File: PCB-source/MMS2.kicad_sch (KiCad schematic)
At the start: 4 parts

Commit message: ch32
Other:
- added sheet CH32V003 (CH32V003.kicad_sch)
- sheet MCU ports: added none; removed CAN_AUTOTERM{1,2}
- sheet STlink-BMprobe ports: added STLINK{UART}; removed none

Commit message: Component placement done
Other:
- sheet Interboard_connector ports: added Altmode[1..16], Chainbus_I2C_addr[0..2], Chainbus_SPI_CS[0..2], Chainbus_UART_addr[0..2], Chainbus{I2C}, Chainbus{SPI}, Chainbus{UART}; removed none
- sheet MCU ports: added Altmode[1..16], Chainbus_I2C_addr[0..2], Chainbus_SPI_CS[0..2], Chainbus_UART_addr[0..2], Chainbus{I2C}, Chainbus{SPI}, Chainbus{UART}; removed none

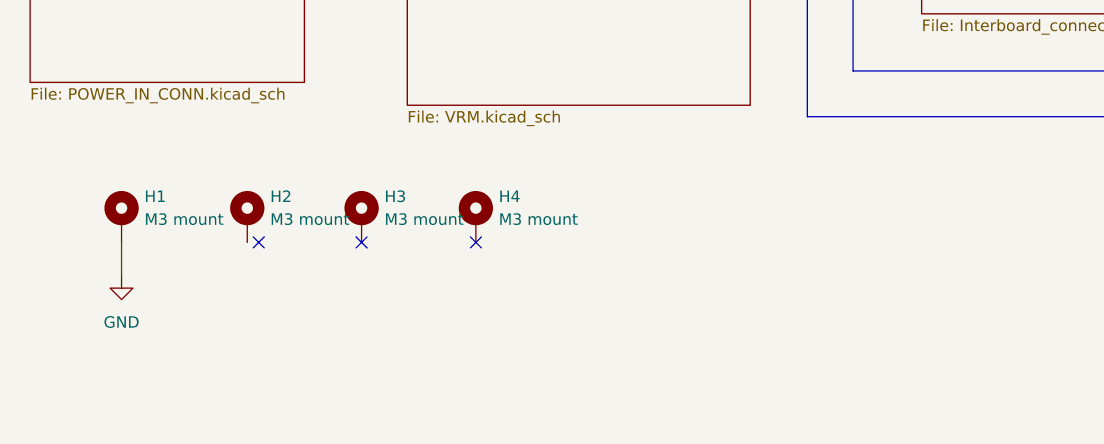
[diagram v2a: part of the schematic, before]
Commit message: processor connection done
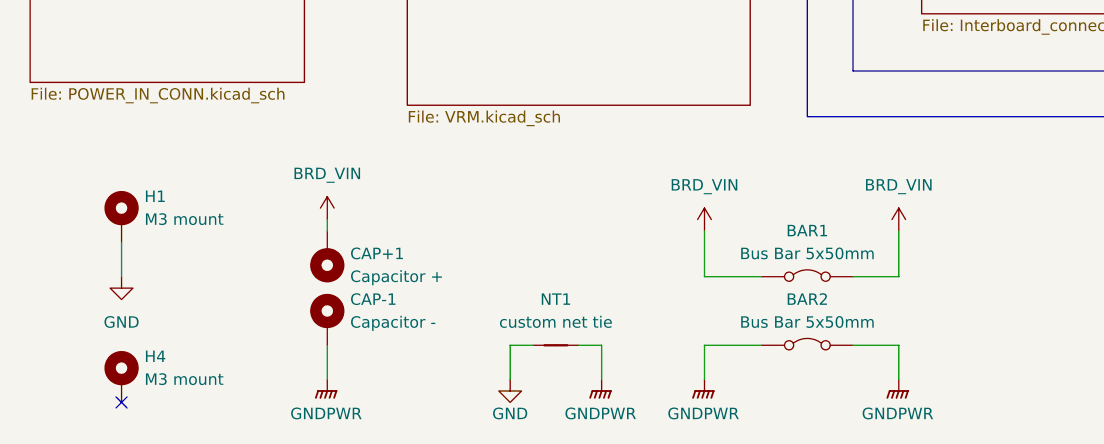
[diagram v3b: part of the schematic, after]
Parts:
- removed H2, H3: M3 mount, MountingHole:MountingHole_3.2mm_M3_DIN965_Pad, symbol Mechanical:MountingHole_Pad
- added BAR1: Bus Bar 5x50mm, BusBar:BusBar-50mm-Red, symbol Jumper:Jumper_2_Bridged
- added BAR2: Bus Bar 5x50mm, BusBar:BusBar-50mm-black, symbol Jumper:Jumper_2_Bridged
- added CAP+1: Capacitor +, TestPoint:TestPoint_THTPad_1.5x1.5mm_Drill0.7mm, symbol Mechanical:MountingHole_Pad
- added CAP-1: Capacitor -, TestPoint:TestPoint_THTPad_1.5x1.5mm_Drill0.7mm, symbol Mechanical:MountingHole_Pad
- added NT1: custom net tie, PgndNetTie:Custom, symbol Device:NetTie_2
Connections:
- net GND: now also NT1.1
- new net BRD_VIN: BAR1.1 (A), BAR1.2 (B), CAP+1.1
- new net GNDPWR: BAR2.1 (A), BAR2.2 (B), CAP-1.1, NT1.2
- no-connect marks 3 -> 1
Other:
- moved on the sheet: H4

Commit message: silk job, signal ratnest done
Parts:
- added NT2: custom net tie, PgndNetTie:SHLD, symbol Device:NetTie_2
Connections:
- net GNDPWR: now also NT2.1
- new net SHLD: NT2.2
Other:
- sheet MCU ports: added none; removed I2C_Memory{I2C}

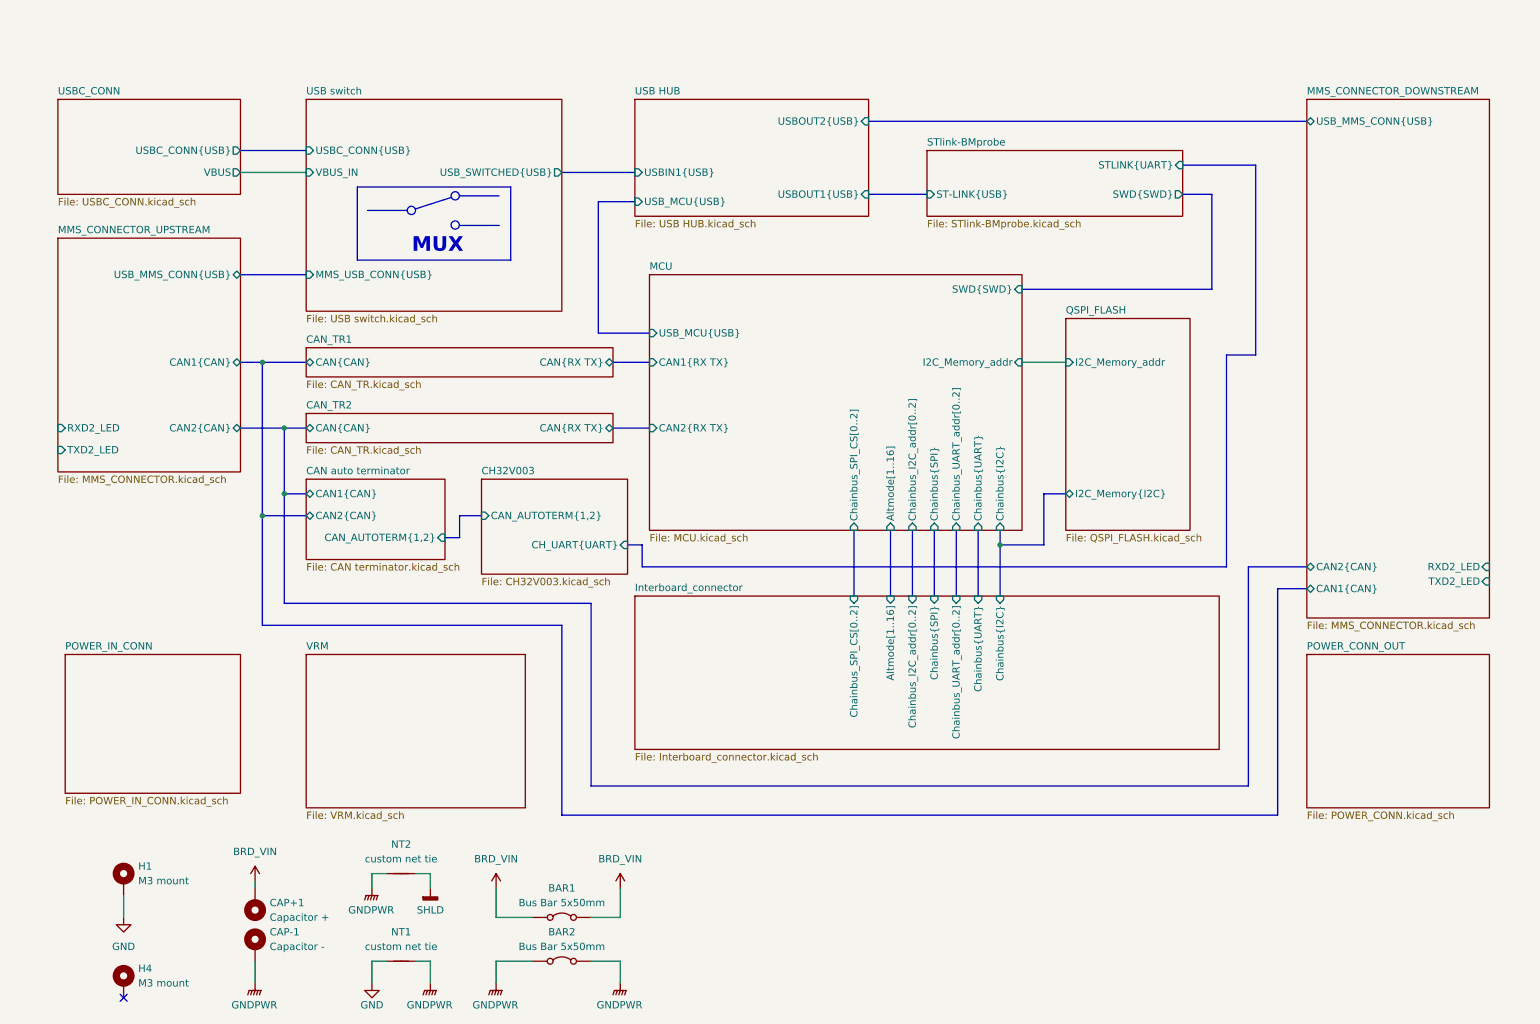
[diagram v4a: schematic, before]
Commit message: change can term add usr led
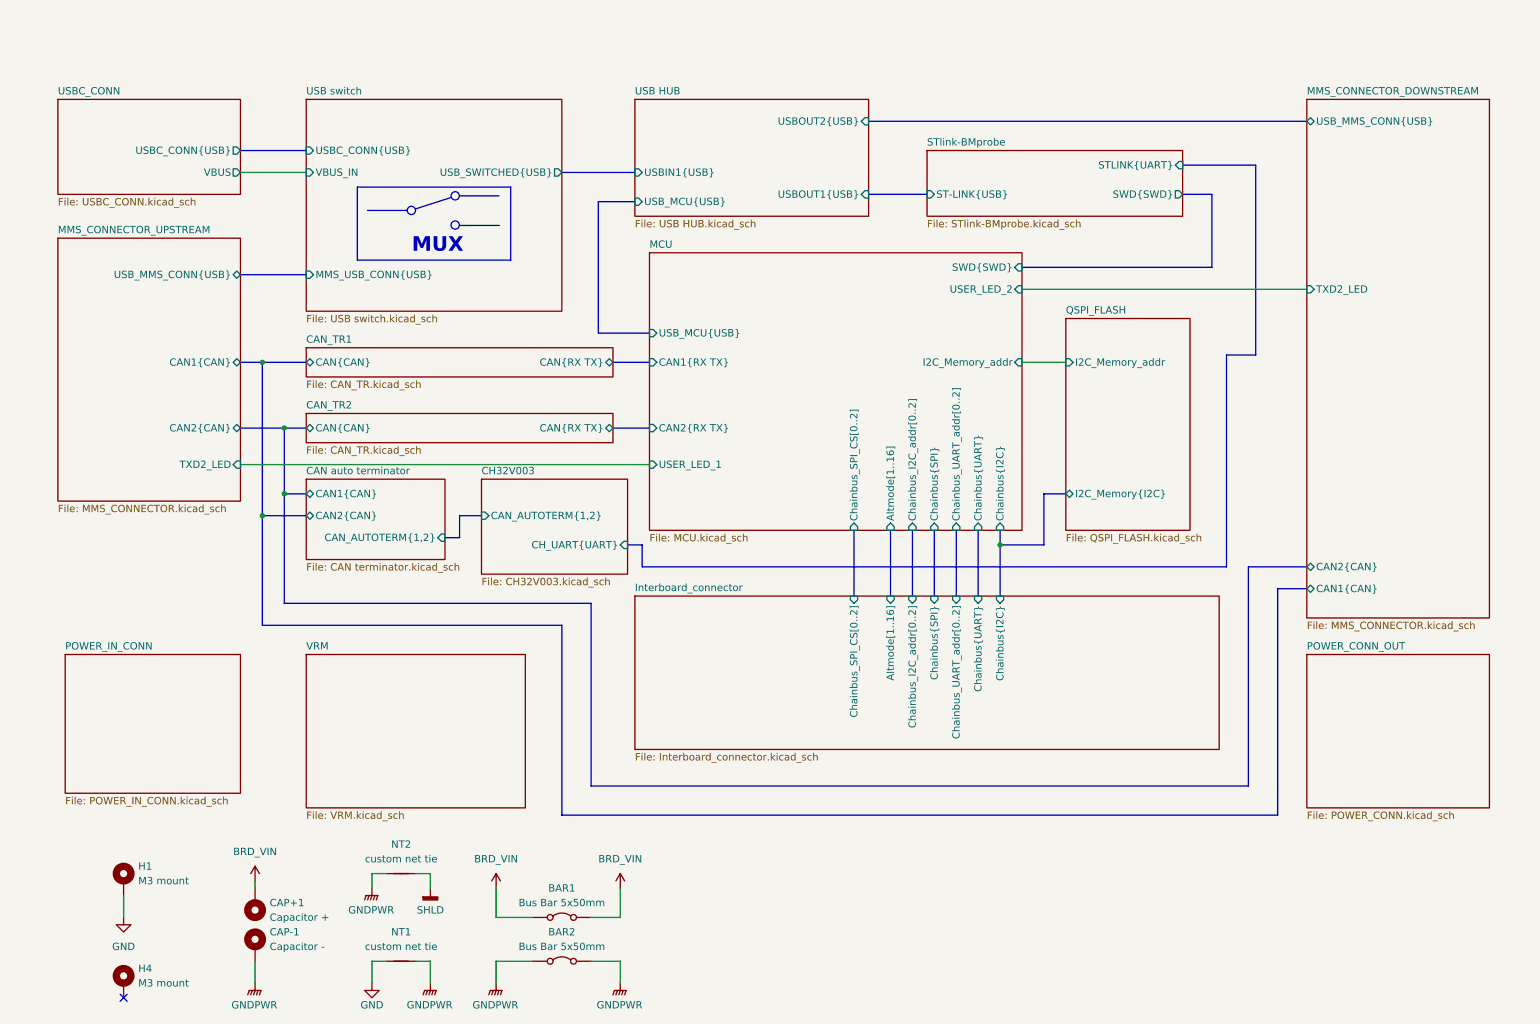
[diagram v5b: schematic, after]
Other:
- sheet MCU ports: added USER_LED_1, USER_LED_2; removed none
- sheet MMS_CONNECTOR_DOWNSTREAM ports: added none; removed RXD2_LED
- sheet MMS_CONNECTOR_UPSTREAM ports: added none; removed RXD2_LED
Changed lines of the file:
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@@
 		)
 	)
+	(wire
+		(pts
+			(xy 191.77 66.04) (xy 241.3 66.04)
+		)
+		(stroke
+			(width 0)
+			(type default)
+		)
+	)
 	(bus
 		(pts
@@
 		)
 	)
+	(wire
+		(pts
+			(xy 55.88 96.52) (xy 127 96.52)
+		)
+		(stroke
+			(width 0)
+			(type default)
+		)
+	)
 	(bus
 		(pts
@@
 	(bus
 		(pts
-			(xy 191.77 66.04) (xy 224.79 66.04)
+			(xy 191.77 62.23) (xy 224.79 62.23)
 		)
 		(stroke
@@
 	(bus
 		(pts
-			(xy 224.79 66.04) (xy 224.79 49.53)
+			(xy 224.79 62.23) (xy 224.79 49.53)
 		)
 		(stroke
@@
 	(sheet
 		(at 24.13 57.15)
-		(size 31.75 40.64)
+		(size 31.75 45.72)
 		(exclude_from_sim no)
 		(in_bom yes)
@@
 		)
 		(property "Sheetfile" "MMS_CONNECTOR.kicad_sch"
-			(at 24.13 98.3746 0)
+			(at 24.13 103.4546 0)
 			(effects
 				(font
@@
 			)
 		)
-		(pin "RXD2_LED" input
-			(at 24.13 90.17 180)
-			(effects
-				(font
-					(size 1.27 1.27)
-				)
-				(justify left)
-			)
-		)
 		(pin "CAN1{CAN}" bidirectional
 			(at 55.88 78.74 0)
@@
 		)
 		(pin "TXD2_LED" input
-			(at 24.13 93.98 180)
+			(at 55.88 96.52 0)
 			(effects
 				(font
 					(size 1.27 1.27)
 				)
-				(justify left)
+				(justify right)
 			)
 		)
@@
 			)
 		)
-		(pin "RXD2_LED" input
-			(at 273.05 114.3 0)
-			(effects
-				(font
-					(size 1.27 1.27)
-				)
-				(justify right)
-			)
-		)
 		(pin "CAN1{CAN}" bidirectional
 			(at 241.3 118.11 180)
@@
 		)
 		(pin "TXD2_LED" input
-			(at 273.05 116.84 0)
+			(at 241.3 66.04 180)
 			(effects
 				(font
 					(size 1.27 1.27)
 				)
-				(justify right)
+				(justify left)
 			)
 		)
@@
 	)
 	(sheet
-		(at 127 63.5)
-		(size 64.77 44.45)
+		(at 127 59.69)
+		(size 64.77 48.26)
 		(exclude_from_sim no)
 		(in_bom yes)
@@
 		)
 		(property "Sheetname" "MCU"
-			(at 127 62.7884 0)
+			(at 127 58.9784 0)
 			(effects
 				(font
@@
 		)
 		(pin "SWD{SWD}" input
-			(at 191.77 66.04 0)
+			(at 191.77 62.23 0)
 			(effects
 				(font
@@
 			)
 		)
+		(pin "USER_LED_1" input
+			(at 127 96.52 180)
+			(effects
+				(font
+					(size 1.27 1.27)
+				)
+				(justify left)
+			)
+		)
+		(pin "USER_LED_2" input
+			(at 191.77 66.04 0)
+			(effects
+				(font
+					(size 1.27 1.27)
+				)
+				(justify right)
+			)
+		)

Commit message: DRC PASS, preparing bom for production
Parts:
- added D6: SS34, PCM_JLCPCB:D_SMA, symbol PCM_JLCPCB-Diodes:Schottky,SS34
- added H2, H3: M3 mount, MountingHole:MountingHole_3.2mm_M3_DIN965_Pad, symbol Mechanical:MountingHole_Pad
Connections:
- net USB switch/VBUS_IN: now also D6.2
- new net +5V: D6.1
- no-connect marks 1 -> 3
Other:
- sheet MMS_CONNECTOR_DOWNSTREAM ports: added RXD2_LED; removed none
- sheet MMS_CONNECTOR_UPSTREAM ports: added RXD2_LED; removed none
- moved on the sheet: CAP-1, H4

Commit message: bom done
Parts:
- BAR1, BAR2: now left out of the parts list
- H3, H4: LCSC (none) -> C49236535; now in the parts list

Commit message: REV A production ready
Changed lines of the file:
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@@
 			)
 		)
-		(property "Footprint" ""
+		(property "Footprint" "QRcode:QR"
 			(at 135.636 183.896 0)
 			(effects
@@
 	(sheet
 		(at 25.4 129.54)
-		(size 30.48 24.13)
+		(size 30.48 26.67)
 		(exclude_from_sim no)
 		(in_bom yes)
@@
 		)
 		(property "Sheetfile" "POWER_IN_CONN.kicad_sch"
-			(at 25.4 154.2546 0)
-			(effects
-				(font
+			(at 25.4 156.7946 0)
+			(effects
+				(font
